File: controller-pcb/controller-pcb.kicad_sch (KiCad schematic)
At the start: 7 parts, among them J1 24V_IN1, J2 24V_IN2, J3 LED_OUT1, J4 LED_OUT2, U1 ESP32-C3_SUPERMINI_SMD, U2 5V_DCDC

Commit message: v1
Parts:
- added J5: INMP441, LEDnet:INMP441_Breakout, symbol LEDnet:INMP441_Breakout
- J1: value 24V_IN1 -> VCC1
- J2: value 24V_IN2 -> VCC2
- J3: value LED_OUT1 -> LED1
- J4: value LED_OUT2 -> LED2
- U2: renamed from U1; value ESP32-C3_SUPERMINI_SMD -> ESP32
- renumbered U2 to U1
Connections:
- net GND: now also J5.1 (GND), J5.4 (L/R)
- net LED2_DATA: now reaches J4.2 (DATA_OUT)
- net LED2_DATA: now also U2.4 (GPIO4); no longer U2.7 (GPIO7)
- net MIC_SD: now reaches U2.10 (GPIO10)
- net MIC_SD: now also J5.3 (SD)
- net LED1_DATA: now reaches U2.3 (GPIO3)
- net LED1_DATA: now also J3.2 (DATA_OUT)
- net +3V3: now reaches U2.3.3 (3V3)
- net +3V3: now also J5.2 (VCC)
- net MIC_SCK: now reaches U2.5 (GPIO5)
- net MIC_SCK: now also J5.6 (SCK)
- net at U2.6 (GPIO6): no longer J3.2 (DATA_OUT)
- new net MIC_WS: J5.5 (WS), U2.7 (GPIO7)
- no-connect marks 12 -> 8
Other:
- moved on the sheet: D1, J2, J3

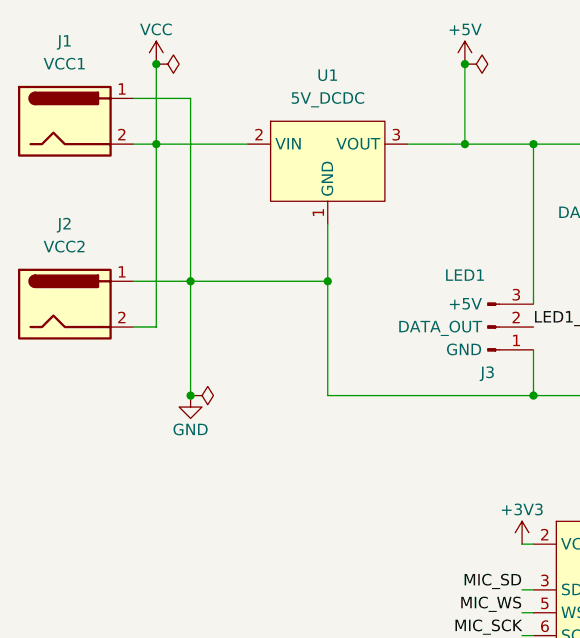
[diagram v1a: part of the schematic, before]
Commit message: fix dc jack polarity
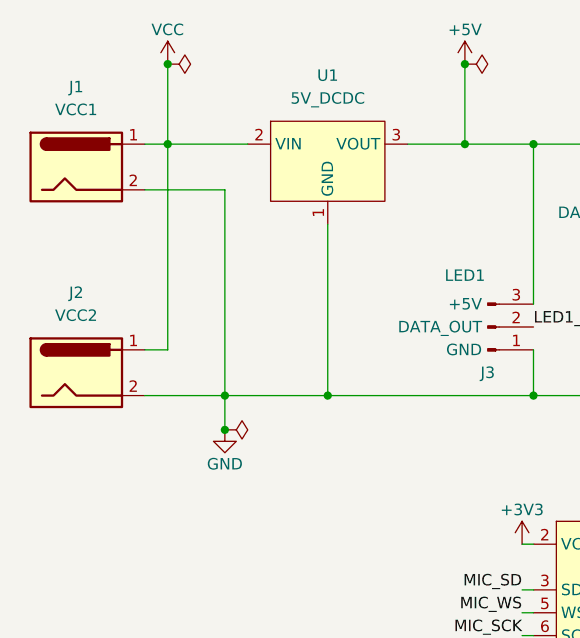
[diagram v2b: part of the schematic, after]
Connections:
- net GND: now also J1.2, J2.2; no longer J1.1, J2.1
- net VCC: now also J1.1, J2.1; no longer J1.2, J2.2
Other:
- moved on the sheet: J1, J2
